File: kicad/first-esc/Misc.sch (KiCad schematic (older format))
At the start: 11 parts

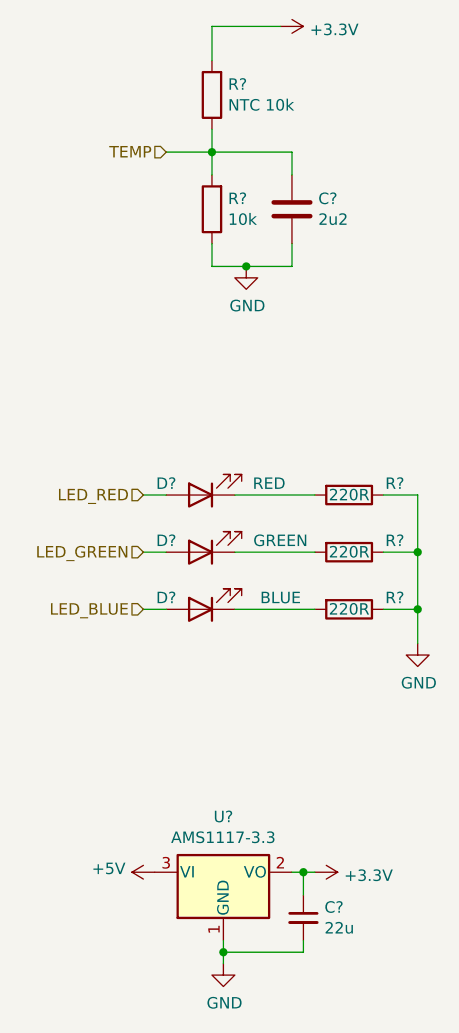
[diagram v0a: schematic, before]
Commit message: mostly finished schematic, started PCB layout
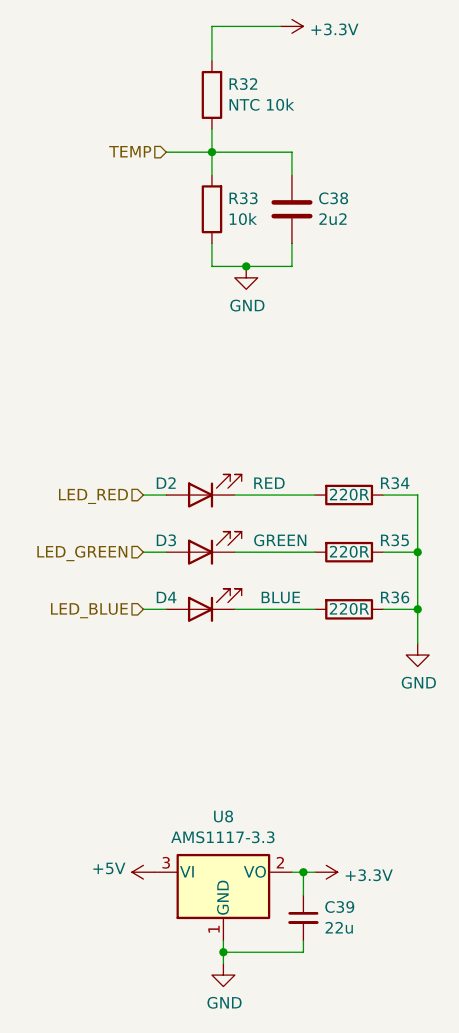
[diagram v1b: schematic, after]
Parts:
- C38: renamed from C?; footprint (none) -> Capacitor_SMD:C_0603_1608Metric
- C39: renamed from C?; footprint (none) -> Capacitor_SMD:C_0805_2012Metric
- D2, D3, D4: renamed from D?; footprint (none) -> LED_SMD:LED_0603_1608Metric
- R32, R33, R34, R35, R36: renamed from R?; footprint (none) -> Resistor_SMD:R_0603_1608Metric
- gave numbers to parts that had none: 1
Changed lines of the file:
@@
 $Descr A4 11693 8268
 encoding utf-8
-Sheet 5 5
+Sheet 4 5
 Title ""
 Date ""
@@
 P 1900 1250
 AR Path="/5FC8DCCF/6006A5AB" Ref="R?"  Part="1"
-AR Path="/60056245/6006A5AB" Ref="R?"  Part="1"
-F 0 "R?" H 1830 1204 50  0000 R CNN
+AR Path="/60056245/6006A5AB" Ref="R32"  Part="1"
+F 0 "R32" H 1830 1204 50  0000 R CNN
 F 1 "NTC 10k" H 1830 1295 50  0000 R CNN
-F 2 "" V 1830 1250 50  0001 C CNN
+F 2 "Resistor_SMD:R_0603_1608Metric" V 1830 1250 50  0001 C CNN
 F 3 "~" H 1900 1250 50  0001 C CNN
 	1    1900 1250
@@
 P 1900 1750
 AR Path="/5FC8DCCF/6006A5B1" Ref="R?"  Part="1"
-AR Path="/60056245/6006A5B1" Ref="R?"  Part="1"
-F 0 "R?" H 1830 1704 50  0000 R CNN
+AR Path="/60056245/6006A5B1" Ref="R33"  Part="1"
+F 0 "R33" H 1830 1704 50  0000 R CNN
 F 1 "10k" H 1830 1795 50  0000 R CNN
-F 2 "" V 1830 1750 50  0001 C CNN
+F 2 "Resistor_SMD:R_0603_1608Metric" V 1830 1750 50  0001 C CNN
 F 3 "~" H 1900 1750 50  0001 C CNN
 	1    1900 1750
@@
 P 2250 1750
 AR Path="/5FC8DCCF/6006A5B7" Ref="C?"  Part="1"
-AR Path="/60056245/6006A5B7" Ref="C?"  Part="1"
-F 0 "C?" H 2365 1796 50  0000 L CNN
+AR Path="/60056245/6006A5B7" Ref="C38"  Part="1"
+F 0 "C38" H 2365 1796 50  0000 L CNN
 F 1 "2u2" H 2365 1705 50  0000 L CNN
-F 2 "" H 2288 1600 50  0001 C CNN
+F 2 "Capacitor_SMD:C_0603_1608Metric" H 2288 1600 50  0001 C CNN
 F 3 "~" H 2250 1750 50  0001 C CNN
 	1    2250 1750
@@
 P 2050 2000
 AR Path="/5FC8DCCF/6006A5BD" Ref="#PWR?"  Part="1"
-AR Path="/60056245/6006A5BD" Ref="#PWR?"  Part="1"
-F 0 "#PWR?" H 2050 1750 50  0001 C CNN
+AR Path="/60056245/6006A5BD" Ref="#PWR0171"  Part="1"
+F 0 "#PWR0171" H 2050 1750 50  0001 C CNN
 F 1 "GND" H 2055 1827 50  0000 C CNN
 F 2 "" H 2050 2000 50  0001 C CNN
@@
 P 2200 950
 AR Path="/5FC8DCCF/6006A5C3" Ref="#PWR?"  Part="1"
-AR Path="/60056245/6006A5C3" Ref="#PWR?"  Part="1"
-F 0 "#PWR?" H 2200 800 50  0001 C CNN
+AR Path="/60056245/6006A5C3" Ref="#PWR0172"  Part="1"
+F 0 "#PWR0172" H 2200 800 50  0001 C CNN
 F 1 "+3.3V" V 2215 1078 50  0000 L CNN
 F 2 "" H 2200 950 50  0001 C CNN
@@
 	2050 2000 1900 2000
 $Comp
-L Device:LED D?
+L Device:LED D2
 U 1 1 6006DDF4
 P 1850 3000
-F 0 "D?" H 2000 2950 50  0000 C CNN
+F 0 "D2" H 2000 2950 50  0000 C CNN
 F 1 "RED" H 1550 2950 50  0000 C CNN
-F 2 "" H 1850 3000 50  0001 C CNN
+F 2 "LED_SMD:LED_0603_1608Metric" H 1850 3000 50  0001 C CNN
 F 3 "~" H 1850 3000 50  0001 C CNN
 	1    1850 3000
@@
 $EndComp
 $Comp
-L Device:LED D?
+L Device:LED D3
 U 1 1 6006F169
 P 1850 3250
-F 0 "D?" H 2000 3200 50  0000 C CNN
+F 0 "D3" H 2000 3200 50  0000 C CNN
 F 1 "GREEN" H 1500 3200 50  0000 C CNN
-F 2 "" H 1850 3250 50  0001 C CNN
+F 2 "LED_SMD:LED_0603_1608Metric" H 1850 3250 50  0001 C CNN
 F 3 "~" H 1850 3250 50  0001 C CNN
 	1    1850 3250
@@
 $EndComp
 $Comp
-L Device:LED D?
+L Device:LED D4
 U 1 1 6006F45B
 P 1850 3500
-F 0 "D?" H 2000 3450 50  0000 C CNN
+F 0 "D4" H 2000 3450 50  0000 C CNN
 F 1 "BLUE" H 1500 3450 50  0000 C CNN
-F 2 "" H 1850 3500 50  0001 C CNN
+F 2 "LED_SMD:LED_0603_1608Metric" H 1850 3500 50  0001 C CNN
 F 3 "~" H 1850 3500 50  0001 C CNN
 	1    1850 3500
@@
 $EndComp
 $Comp
-L Device:R R?
+L Device:R R34
 U 1 1 60070069
 P 2500 3000
-F 0 "R?" V 2450 3200 50  0000 C CNN
+F 0 "R34" V 2450 3200 50  0000 C CNN
 F 1 "220R" V 2500 3000 50  0000 C CNN
-F 2 "" V 2430 3000 50  0001 C CNN
+F 2 "Resistor_SMD:R_0603_1608Metric" V 2430 3000 50  0001 C CNN
 F 3 "~" H 2500 3000 50  0001 C CNN
 	1    2500 3000
@@
 $EndComp
 $Comp
-L Device:R R?
+L Device:R R35
 U 1 1 60070A92
 P 2500 3250
-F 0 "R?" V 2450 3450 50  0000 C CNN
+F 0 "R35" V 2450 3450 50  0000 C CNN
 F 1 "220R" V 2500 3250 50  0000 C CNN
-F 2 "" V 2430 3250 50  0001 C CNN
+F 2 "Resistor_SMD:R_0603_1608Metric" V 2430 3250 50  0001 C CNN
 F 3 "~" H 2500 3250 50  0001 C CNN
 	1    2500 3250
@@
 $EndComp
 $Comp
-L Device:R R?
+L Device:R R36
 U 1 1 60070E4F
 P 2500 3500
-F 0 "R?" V 2450 3700 50  0000 C CNN
+F 0 "R36" V 2450 3700 50  0000 C CNN
 F 1 "220R" V 2500 3500 50  0000 C CNN
-F 2 "" V 2430 3500 50  0001 C CNN
+F 2 "Resistor_SMD:R_0603_1608Metric" V 2430 3500 50  0001 C CNN
 F 3 "~" H 2500 3500 50  0001 C CNN
 	1    2500 3500
@@
 P 2800 3650
 AR Path="/5FC8DCCF/60072BC1" Ref="#PWR?"  Part="1"
-AR Path="/60056245/60072BC1" Ref="#PWR?"  Part="1"
-F 0 "#PWR?" H 2800 3400 50  0001 C CNN
+AR Path="/60056245/60072BC1" Ref="#PWR0173"  Part="1"
+F 0 "#PWR0173" H 2800 3400 50  0001 C CNN
 F 1 "GND" H 2805 3477 50  0000 C CNN
 F 2 "" H 2800 3650 50  0001 C CNN
@@
 	1600 3500 1700 3500
 $Comp
-L Regulator_Linear:AMS1117-3.3 U?
+L Regulator_Linear:AMS1117-3.3 U8
 U 1 1 600753AF
 P 1950 4650
-F 0 "U?" H 1950 4892 50  0000 C CNN
+F 0 "U8" H 1950 4892 50  0000 C CNN
 F 1 "AMS1117-3.3" H 1950 4801 50  0000 C CNN
 F 2 "Package_TO_SOT_SMD:SOT-223-3_TabPin2" H 1950 4850 50  0001 C CNN
@@
 P 1950 5050
 AR Path="/5FC8DCCF/60075D71" Ref="#PWR?"  Part="1"
-AR Path="/60056245/60075D71" Ref="#PWR?"  Part="1"
-F 0 "#PWR?" H 1950 4800 50  0001 C CNN
+AR Path="/60056245/60075D71" Ref="#PWR0174"  Part="1"
+F 0 "#PWR0174" H 1950 4800 50  0001 C CNN
 F 1 "GND" H 1955 4877 50  0000 C CNN
 F 2 "" H 1950 5050 50  0001 C CNN
@@
 $EndComp
 $Comp
-L power:+5V #PWR?
+L power:+5V #PWR0175
 U 1 1 60077BD4
 P 1650 4650
-F 0 "#PWR?" H 1650 4500 50  0001 C CNN
+F 0 "#PWR0175" H 1650 4500 50  0001 C CNN
 F 1 "+5V" V 1665 4778 50  0000 L CNN
 F 2 "" H 1650 4650 50  0001 C CNN
@@
 $EndComp
 $Comp
-L power:+3.3V #PWR?
+L power:+3.3V #PWR0176
 U 1 1 600789DB
 P 2350 4650
-F 0 "#PWR?" H 2350 4500 50  0001 C CNN
+F 0 "#PWR0176" H 2350 4500 50  0001 C CNN
 F 1 "+3.3V" V 2365 4778 50  0000 L CNN
 F 2 "" H 2350 4650 50  0001 C CNN
@@
 $EndComp
 $Comp
-L Device:C_Small C?
+L Device:C_Small C39
 U 1 1 60079747
 P 2300 4850
-F 0 "C?" H 2392 4896 50  0000 L CNN
+F 0 "C39" H 2392 4896 50  0000 L CNN
 F 1 "22u" H 2392 4805 50  0000 L CNN
-F 2 "" H 2300 4850 50  0001 C CNN
+F 2 "Capacitor_SMD:C_0805_2012Metric" H 2300 4850 50  0001 C CNN
 F 3 "~" H 2300 4850 50  0001 C CNN
 	1    2300 4850
